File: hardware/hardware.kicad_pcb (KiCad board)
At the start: 2 copper layers, 91.4 x 91.4 mm, 104 parts, among them J1 DB25_Female, J2 USB_B_Micro, J3 RJ45_Bel_SI-60062-F-68net, J4 Conn_01x02_Male, J5 Conn_01x02_Male, U1 MIC5319, U11 ENC28J60x-SO, U12 74LVC14, U2 74LVTH126, U3 74LVTH126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

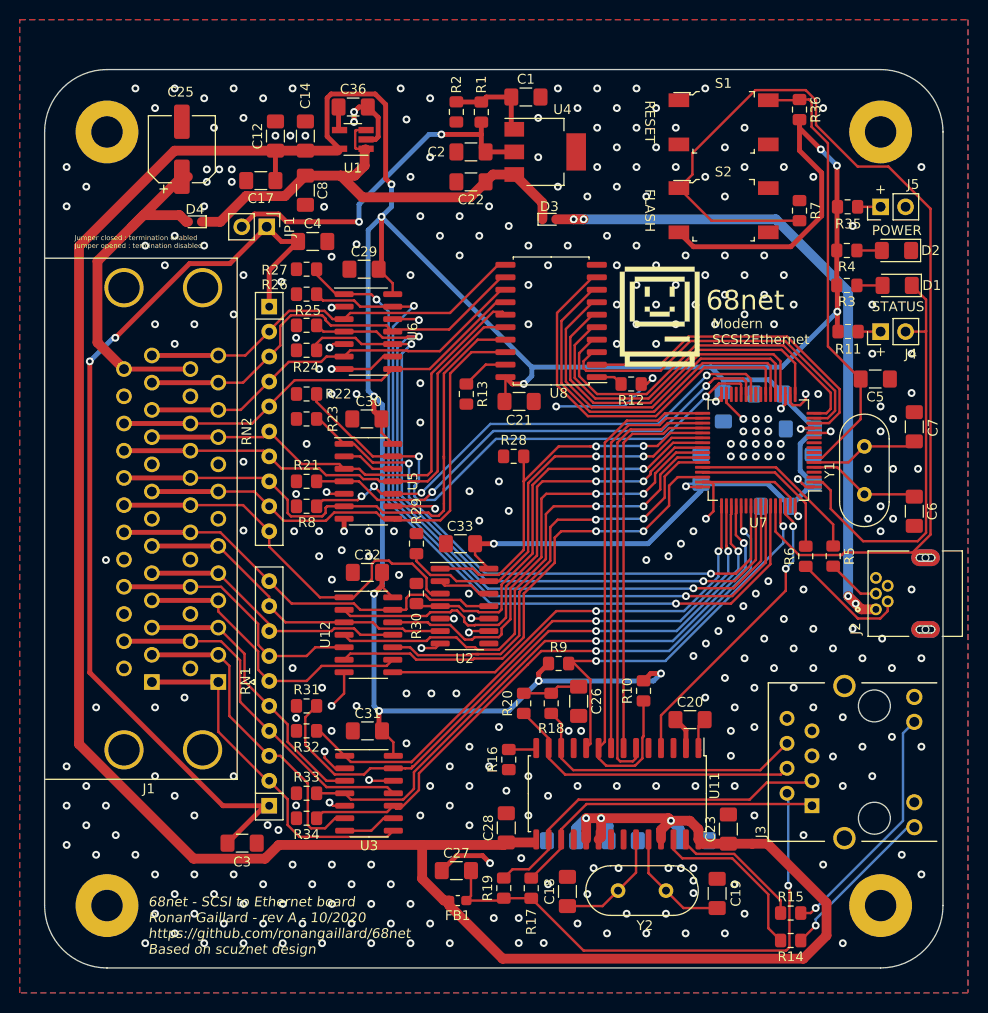
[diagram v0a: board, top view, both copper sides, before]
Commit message: feat: add JLCJLC... +fix trace touching usb shield
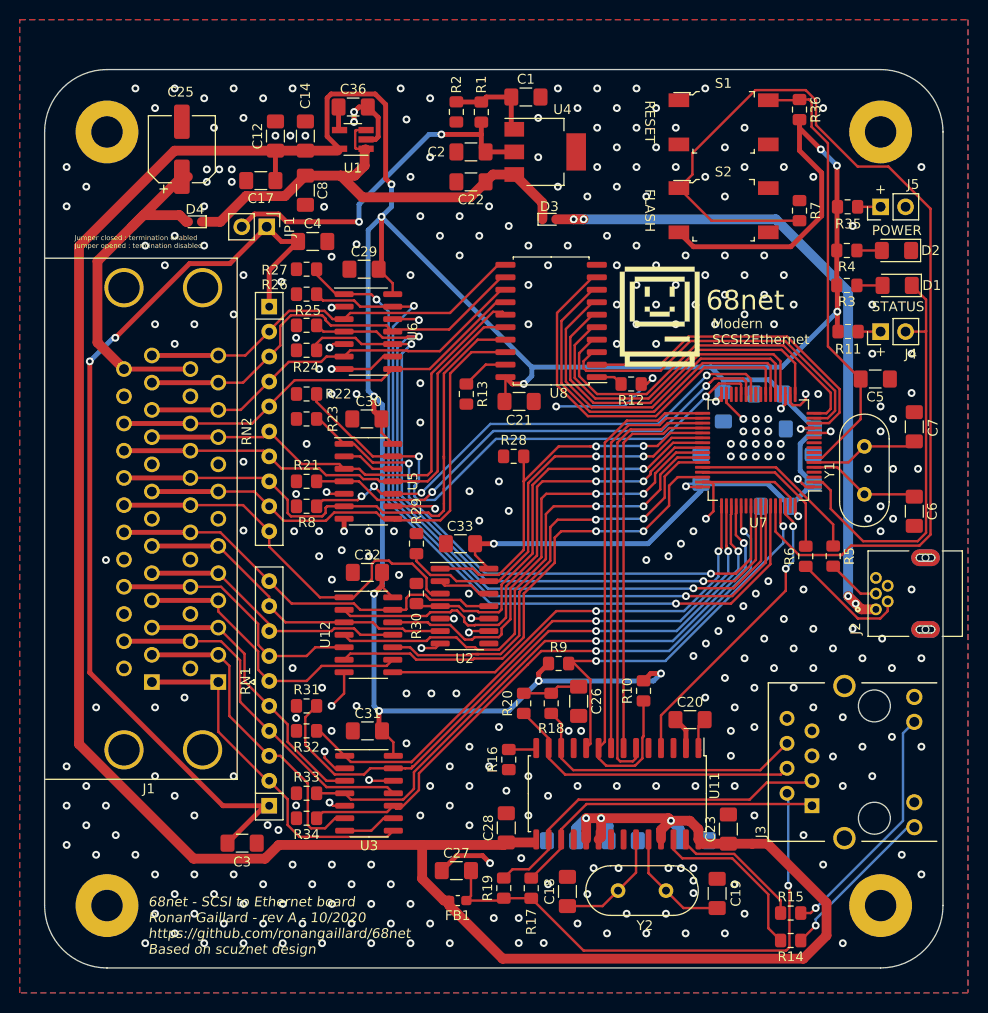
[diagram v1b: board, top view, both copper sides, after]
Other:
- board text added: "JLCJLCJLCJLC"
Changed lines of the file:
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@@
   (general
     (thickness 1.6)
-    (drawings 18)
+    (drawings 19)
     (tracks 1585)
     (zones 0)
@@
     (visible_elements FFFFFFFF)
     (pcbplotparams
-      (layerselection 0x010fc_ffffffff)
+      (layerselection 0x310fc_ffffffff)
       (usegerberextensions false)
       (usegerberattributes true)
@@
       (drillshape 0)
       (scaleselection 1)
-      (outputdirectory ""))
+      (outputdirectory "revA/"))
   )
   (net 0 "")
@@
       (effects (font (size 1 1) (thickness 0.15)))
     )
-    (fp_text user %R (at 0 0 90) (layer F.Fab)
-      (effects (font (size 0.5 0.5) (thickness 0.08)))
-    )
     (fp_line (start -1 0.6) (end -1 -0.6) (layer F.Fab) (width 0.1))
     (fp_line (start -1 -0.6) (end 1 -0.6) (layer F.Fab) (width 0.1))
@@
     (fp_line (start 1.85 -0.95) (end 1.85 0.95) (layer F.CrtYd) (width 0.05))
     (fp_line (start 1.85 0.95) (end -1.85 0.95) (layer F.CrtYd) (width 0.05))
-    (pad 2 smd roundrect (at 1.025 0 90) (size 1.15 1.4) (layers F.Cu F.Paste F.Mask) (roundrect_rratio 0.217391)
+    (fp_text user %R (at 0 0 90) (layer F.Fab)
+      (effects (font (size 0.5 0.5) (thickness 0.08)))
+    )
+    (pad 2 smd roundrect (at 1.025 0 90) (size 1.15 1.4) (layers F.Cu F.Paste F.Mask) (roundrect_rratio 0.2173904347826087)
       (net 4 /NRST))
-    (pad 1 smd roundrect (at -1.025 0 90) (size 1.15 1.4) (layers F.Cu F.Paste F.Mask) (roundrect_rratio 0.217391)
+    (pad 1 smd roundrect (at -1.025 0 90) (size 1.15 1.4) (layers F.Cu F.Paste F.Mask) (roundrect_rratio 0.2173904347826087)
       (net 8 +3V3))
     (model ${KISYS3DMOD}/Resistor_SMD.3dshapes/R_0805_2012Metric.wrl
@@
       (effects (font (size 0.5 0.5) (thickness 0.08)))
     )
-    (pad 2 smd roundrect (at 1.025 0 180) (size 1.15 1.4) (layers F.Cu F.Paste F.Mask) (roundrect_rratio 0.217391)
+    (pad 2 smd roundrect (at 1.025 0 180) (size 1.15 1.4) (layers F.Cu F.Paste F.Mask) (roundrect_rratio 0.2173904347826087)
       (net 8 +3V3))
-    (pad 1 smd roundrect (at -1.025 0 180) (size 1.15 1.4) (layers F.Cu F.Paste F.Mask) (roundrect_rratio 0.217391)
+    (pad 1 smd roundrect (at -1.025 0 180) (size 1.15 1.4) (layers F.Cu F.Paste F.Mask) (roundrect_rratio 0.2173904347826087)
       (net 112 "Net-(J5-Pad1)"))
     (model ${KISYS3DMOD}/Resistor_SMD.3dshapes/R_0805_2012Metric.wrl
@@
       (effects (font (size 0.5 0.5) (thickness 0.08)))
     )
-    (pad 2 smd roundrect (at 1.025 0 180) (size 1.15 1.4) (layers F.Cu F.Paste F.Mask) (roundrect_rratio 0.217391)
+    (pad 2 smd roundrect (at 1.025 0 180) (size 1.15 1.4) (layers F.Cu F.Paste F.Mask) (roundrect_rratio 0.2173904347826087)
       (net 8 +3V3))
-    (pad 1 smd roundrect (at -1.025 0 180) (size 1.15 1.4) (layers F.Cu F.Paste F.Mask) (roundrect_rratio 0.217391)
+    (pad 1 smd roundrect (at -1.025 0 180) (size 1.15 1.4) (layers F.Cu F.Paste F.Mask) (roundrect_rratio 0.2173904347826087)
       (net 111 "Net-(J4-Pad1)"))
     (model ${KISYS3DMOD}/Resistor_SMD.3dshapes/R_0805_2012Metric.wrl
@@
       (effects (font (size 0.8 0.8) (thickness 0.12)))
     )
-    (pad 2 smd roundrect (at 1.4875 0) (size 1.425 1.75) (layers F.Cu F.Paste F.Mask) (roundrect_rratio 0.175439)
+    (pad 2 smd roundrect (at 1.4875 0) (size 1.425 1.75) (layers F.Cu F.Paste F.Mask) (roundrect_rratio 0.1754385964912281)
       (net 1 GND))
-    (pad 1 smd roundrect (at -1.4875 0) (size 1.425 1.75) (layers F.Cu F.Paste F.Mask) (roundrect_rratio 0.175439)
+    (pad 1 smd roundrect (at -1.4875 0) (size 1.425 1.75) (layers F.Cu F.Paste F.Mask) (roundrect_rratio 0.1754385964912281)
       (net 110 "Net-(C36-Pad1)"))
     (model ${KISYS3DMOD}/Capacitor_SMD.3dshapes/C_1206_3216Metric.wrl
@@
       (effects (font (size 0.8 0.8) (thickness 0.12)) (justify mirror))
     )
-    (pad 2 smd roundrect (at 1.4875 0 180) (size 1.425 1.75) (layers B.Cu B.Paste B.Mask) (roundrect_rratio 0.175439)
+    (pad 2 smd roundrect (at 1.4875 0 180) (size 1.425 1.75) (layers B.Cu B.Paste B.Mask) (roundrect_rratio 0.1754385964912281)
       (net 1 GND))
-    (pad 1 smd roundrect (at -1.4875 0 180) (size 1.425 1.75) (layers B.Cu B.Paste B.Mask) (roundrect_rratio 0.175439)
+    (pad 1 smd roundrect (at -1.4875 0 180) (size 1.425 1.75) (layers B.Cu B.Paste B.Mask) (roundrect_rratio 0.1754385964912281)
       (net 8 +3V3))
     (model ${KISYS3DMOD}/Capacitor_SMD.3dshapes/C_1206_3216Metric.wrl
@@
       (effects (font (size 0.8 0.8) (thickness 0.12)) (justify mirror))
     )
-    (pad 2 smd roundrect (at 1.4875 0) (size 1.425 1.75) (layers B.Cu B.Paste B.Mask) (roundrect_rratio 0.175439)
+    (pad 2 smd roundrect (at 1.4875 0) (size 1.425 1.75) (layers B.Cu B.Paste B.Mask) (roundrect_rratio 0.1754385964912281)
       (net 1 GND))
-    (pad 1 smd roundrect (at -1.4875 0) (size 1.425 1.75) (layers B.Cu B.Paste B.Mask) (roundrect_rratio 0.175439)
+    (pad 1 smd roundrect (at -1.4875 0) (size 1.425 1.75) (layers B.Cu B.Paste B.Mask) (roundrect_rratio 0.1754385964912281)
       (net 8 +3V3))
     (model ${KISYS3DMOD}/Capacitor_SMD.3dshapes/C_1206_3216Metric.wrl
@@
       (effects (font (size 0.8 0.8) (thickness 0.12)))
     )
-    (pad 2 smd roundrect (at 1.4875 0 90) (size 1.425 1.75) (layers F.Cu F.Paste F.Mask) (roundrect_rratio 0.175439)
+    (pad 2 smd roundrect (at 1.4875 0 90) (size 1.425 1.75) (layers F.Cu F.Paste F.Mask) (roundrect_rratio 0.1754385964912281)
       (net 1 GND))
-    (pad 1 smd roundrect (at -1.4875 0 90) (size 1.425 1.75) (layers F.Cu F.Paste F.Mask) (roundrect_rratio 0.175439)
+    (pad 1 smd roundrect (at -1.4875 0 90) (size 1.425 1.75) (layers F.Cu F.Paste F.Mask) (roundrect_rratio 0.1754385964912281)
       (net 8 +3V3))
     (model ${KISYS3DMOD}/Capacitor_SMD.3dshapes/C_1206_3216Metric.wrl
@@
     )
   )
+  (gr_text JLCJLCJLCJLC (at 39.243 107.95) (layer B.SilkS)
+    (effects (font (size 1 1) (thickness 0.2)) (justify mirror))
+  )
   (gr_text + (at 105.41 32.512) (layer F.SilkS)
     (effects (font (size 1 1) (thickness 0.2)))
@@
   (segment (start 71.628 90.404) (end 73.30304 92.07904) (width 0.25) (layer F.Cu) (net 51))
   (segment (start 71.628 89.379) (end 71.628 90.404) (width 0.25) (layer F.Cu) (net 51))
-  (segment (start 97.790189 22.414999) (end 92.669999 22.414999) (width 0.25) (layer F.Cu) (net 52))
-  (segment (start 98.837499 23.462309) (end 97.790189 22.414999) (width 0.25) (layer F.Cu) (net 52))
-  (segment (start 106.204003 30.195001) (end 103.070003 30.195001) (width 0.25) (layer F.Cu) (net 52))
-  (segment (start 94.714 64.73) (end 94.714 67.34619) (width 0.25) (layer F.Cu) (net 52))
-  (segment (start 110.489019 34.480017) (end 106.204003 30.195001) (width 0.25) (layer F.Cu) (net 52))
-  (segment (start 110.489019 67.652581) (end 110.489019 34.480017) (width 0.25) (layer F.Cu) (net 52))
-  (segment (start 92.669999 22.414999) (end 86.255001 28.829997) (width 0.25) (layer F.Cu) (net 52))
-  (segment (start 108.666601 69.474999) (end 110.489019 67.652581) (width 0.25) (layer F.Cu) (net 52))
-  (segment (start 86.255001 28.829997) (end 86.255001 31.009999) (width 0.25) (layer F.Cu) (net 52))
-  (segment (start 94.714 67.34619) (end 97.10182 69.73401) (width 0.25) (layer F.Cu) (net 52))
-  (segment (start 101.721001 69.474999) (end 108.666601 69.474999) (width 0.25) (layer F.Cu) (net 52))
-  (segment (start 86.255001 31.009999) (end 84.88 32.385) (width 0.25) (layer F.Cu) (net 52))
-  (segment (start 98.837499 25.962497) (end 98.837499 23.462309) (width 0.25) (layer F.Cu) (net 52))
-  (segment (start 101.46199 69.73401) (end 101.721001 69.474999) (width 0.25) (layer F.Cu) (net 52))
-  (segment (start 103.070003 30.195001) (end 98.837499 25.962497) (width 0.25) (layer F.Cu) (net 52))
-  (segment (start 97.10182 69.73401) (end 101.46199 69.73401) (width 0.25) (layer F.Cu) (net 52))
   (segment (start 88.2 35.705) (end 84.88 32.385) (width 0.25) (layer F.Cu) (net 52))
   (segment (start 97.155 35.705) (end 88.2 35.705) (width 0.25) (layer F.Cu) (net 52))
+  (segment (start 94.714 67.34619) (end 94.714 64.73) (width 0.25) (layer F.Cu) (net 52))
+  (segment (start 97.10182 69.73401) (end 94.714 67.34619) (width 0.25) (layer F.Cu) (net 52))
+  (segment (start 101.46199 69.73401) (end 97.10182 69.73401) (width 0.25) (layer F.Cu) (net 52))
+  (segment (start 102.41999 68.77601) (end 101.46199 69.73401) (width 0.25) (layer F.Cu) (net 52))
+  (segment (start 109.36559 68.77601) (end 102.41999 68.77601) (width 0.25) (layer F.Cu) (net 52))
+  (segment (start 110.489019 34.480017) (end 110.489019 67.652581) (width 0.25) (layer F.Cu) (net 52))
+  (segment (start 106.204003 30.195001) (end 110.489019 34.480017) (width 0.25) (layer F.Cu) (net 52))
+  (segment (start 110.489019 67.652581) (end 109.36559 68.77601) (width 0.25) (layer F.Cu) (net 52))
+  (segment (start 98.837499 25.962497) (end 103.070003 30.195001) (width 0.25) (layer F.Cu) (net 52))
+  (segment (start 98.837499 23.462309) (end 98.837499 25.962497) (width 0.25) (layer F.Cu) (net 52))
+  (segment (start 86.255001 31.009999) (end 86.255001 28.829997) (width 0.25) (layer F.Cu) (net 52))
+  (segment (start 97.790189 22.414999) (end 98.837499 23.462309) (width 0.25) (layer F.Cu) (net 52))
+  (segment (start 86.255001 28.829997) (end 92.669999 22.414999) (width 0.25) (layer F.Cu) (net 52))
+  (segment (start 92.669999 22.414999) (end 97.790189 22.414999) (width 0.25) (layer F.Cu) (net 52))
+  (segment (start 103.070003 30.195001) (end 106.204003 30.195001) (width 0.25) (layer F.Cu) (net 52))
+  (segment (start 84.88 32.385) (end 86.255001 31.009999) (width 0.25) (layer F.Cu) (net 52))
   (via (at 57.658 48.26) (size 0.8) (drill 0.4) (layers F.Cu B.Cu) (net 53))
   (segment (start 55.75 48.26) (end 57.658 48.26) (width 0.25) (layer F.Cu) (net 53))
